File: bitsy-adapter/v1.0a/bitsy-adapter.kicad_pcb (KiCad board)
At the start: 2 copper layers, 63.5 x 31.8 mm, 17 parts, among them J1 PMOD1, J2 PMOD2, J3 PMOD3, J4 5V AUX, J5 5V AUX

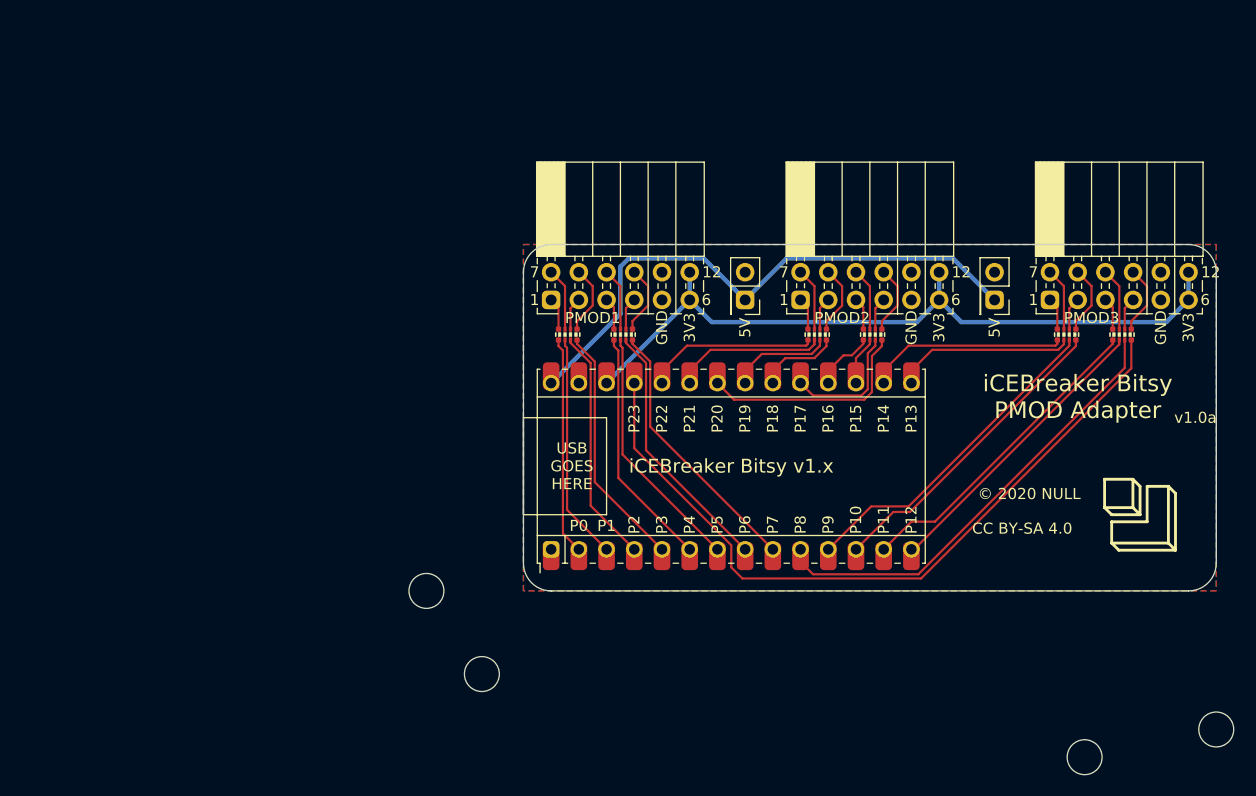
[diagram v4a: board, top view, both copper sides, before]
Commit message: Bitsy Adapter: change formfactor
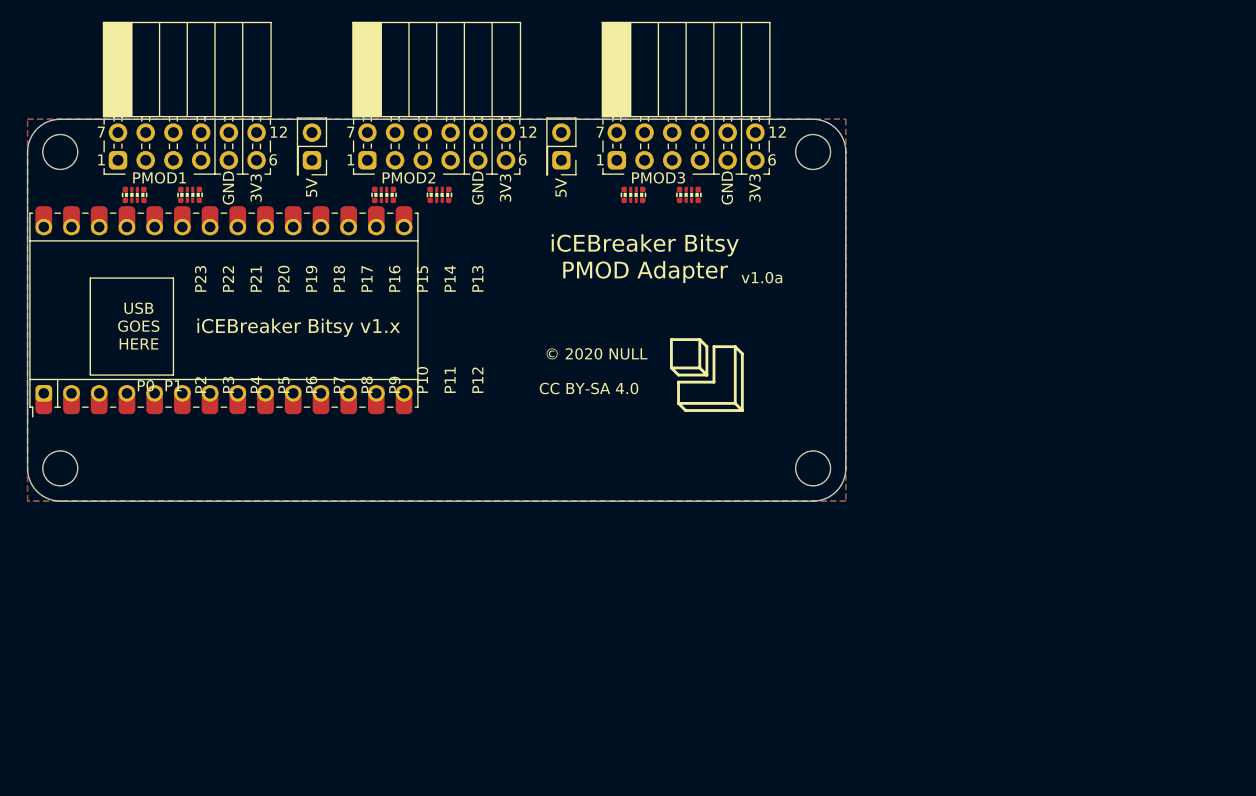
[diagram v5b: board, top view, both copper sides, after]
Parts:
- moved H2 109.0 mm to (65.5, 85.5)
- moved H4 56.7 mm to (134.5, 85.5)
- moved A1 48.6 mm to (80.5, 100.0)
- moved H3 44.0 mm to (134.5, 114.5)
- moved J4 41.7 mm to (88.6, 86.3)
- moved LOGO1 41.7 mm to (124.8, 105.9)
- moved J3 41.7 mm to (116.5, 86.3)
- moved R1 41.7 mm to (72.3, 89.4)
- moved R4 41.7 mm to (100.3, 89.4)
- moved R5 41.7 mm to (118.0, 89.4)
- moved J1 41.7 mm to (70.8, 86.3)
- moved J2 41.7 mm to (93.7, 86.3)
- moved J5 41.7 mm to (111.4, 86.3)
- moved R2 41.7 mm to (77.4, 89.4)
- moved R3 41.7 mm to (95.2, 89.4)
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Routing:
- net /P23: track 68.2 -> 0.00 mm
- net +3V3: track 67.5 -> 0.00 mm
- net +5V: track 52.6 -> 0.00 mm
- net /P8: track 41.1 -> 0.00 mm
- net /P9: track 30.3 -> 0.00 mm
- net /P11: track 29.1 -> 0.00 mm
- net /P10: track 28.4 -> 0.00 mm
- net /P12: track 27.2 -> 0.00 mm
- net /P7: track 24.5 -> 0.00 mm
- net /P6: track 23.7 -> 0.00 mm
- net /P5: track 22.9 -> 0.00 mm
- net /P3: track 22.4 -> 0.00 mm
- net /P4: track 22.1 -> 0.00 mm
- net /P2: track 21.6 -> 0.00 mm
- net /P1: track 20.8 -> 0.00 mm
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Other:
- board size 63.5 x 31.8 mm -> 75 x 35 mm

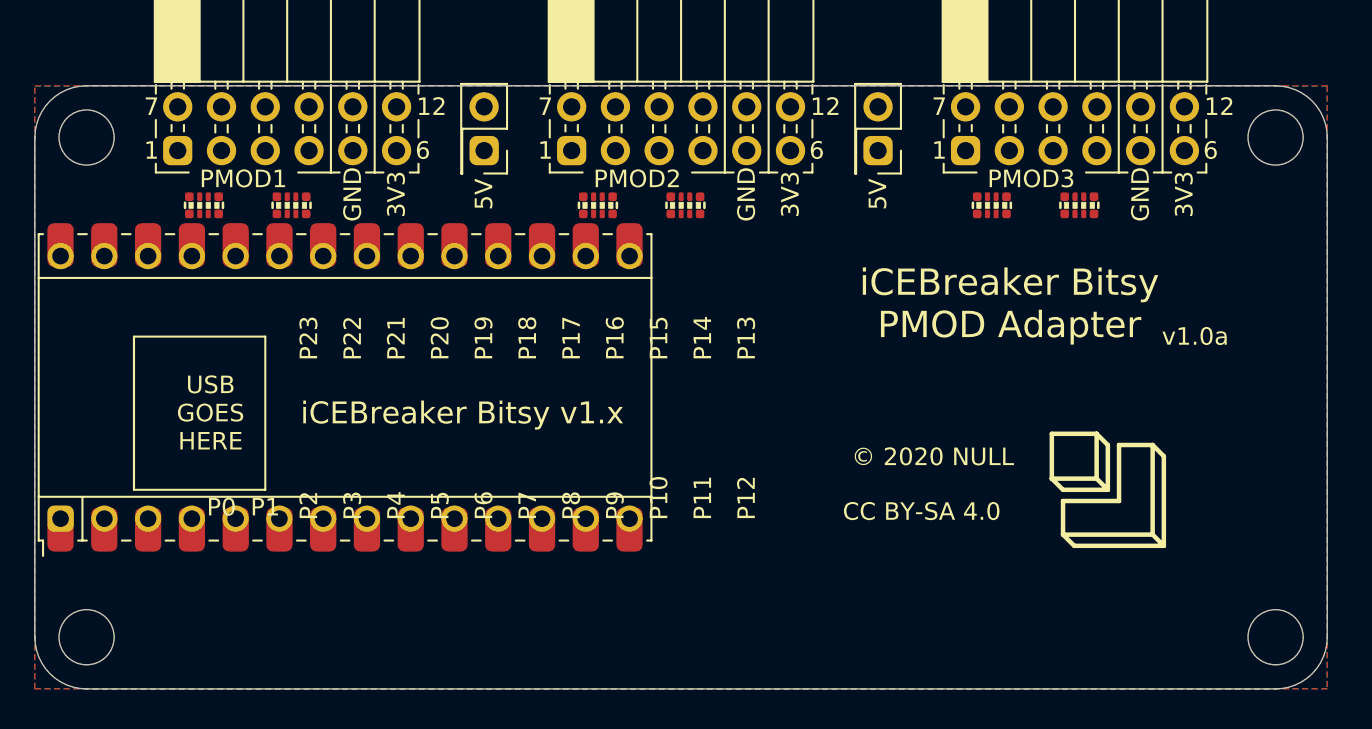
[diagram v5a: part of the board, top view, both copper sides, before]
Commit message: Bitsy Adapter: finish v1.0a
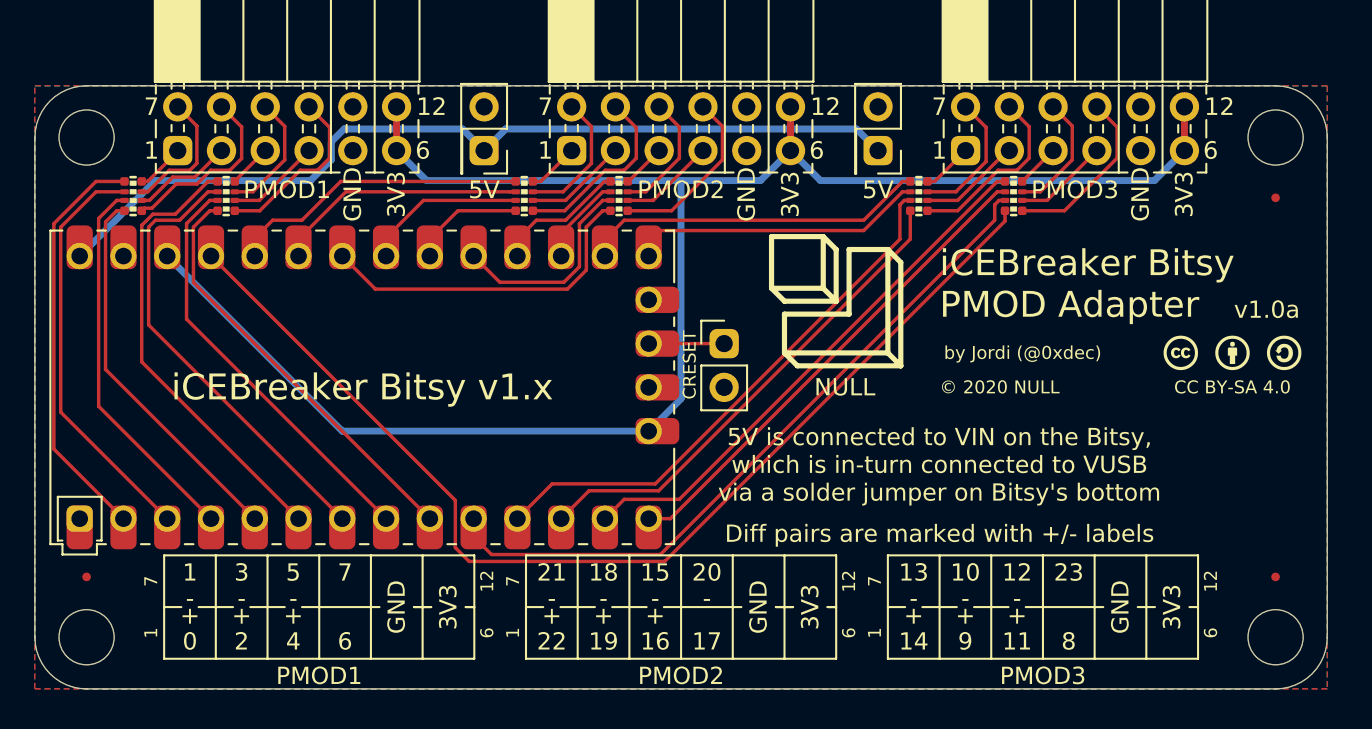
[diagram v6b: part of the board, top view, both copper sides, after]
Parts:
- added FID1: Fiducial, Fiducial:Fiducial_0.5mm_Mask1.5mm, F.Cu at (65.5, 111.0)
- added FID2: Fiducial, Fiducial:Fiducial_0.5mm_Mask1.5mm, F.Cu at (134.5, 111.0)
- added FID3: Fiducial, Fiducial:Fiducial_0.5mm_Mask1.5mm, F.Cu at (134.5, 89.0)
- added JP1: CRESET, Connector_PinHeader_2.54mm:PinHeader_1x02_P2.54mm_Vertical, F.Cu at (102.5, 97.5)
- added REF**: 1b2_Logo_SilkS_7.5mm, pkl_logos:1b2_Logo_SilkS_7.5mm, B.Cu at (132.0, 95.0)
- added REF**: Symbol_CC-SA_SilkScreen_2mm, pkl_logos:Symbol_CC-SA_SilkScreen_2mm, B.Cu at (106.0, 98.0)
- added REF**: Symbol_CC-BY_SilkScreen_2mm, pkl_logos:Symbol_CC-BY_SilkScreen_2mm, B.Cu at (109.0, 98.0)
- added REF**: Symbol_CC_SilkScreen_2mm, pkl_logos:Symbol_CC_SilkScreen_2mm, B.Cu at (112.0, 98.0)
- added REF**: Symbol_CC-SA_SilkScreen_2mm, pkl_logos:Symbol_CC-SA_SilkScreen_2mm, F.Cu at (135.0, 98.0)
- added REF**: Symbol_CC-BY_SilkScreen_2mm, pkl_logos:Symbol_CC-BY_SilkScreen_2mm, F.Cu at (132.0, 98.0)
- added REF**: Symbol_CC_SilkScreen_2mm, pkl_logos:Symbol_CC_SilkScreen_2mm, F.Cu at (129.0, 98.0)
- LOGO1: footprint pkl_logos:1b2_Logo_SilkS_6.5mm -> pkl_logos:1b2_Logo_SilkS_7.5mm
- moved LOGO1 19.2 mm to (109.0, 95.0)
- moved R3 4.31 mm to (90.9, 88.9), turned to 0 degrees
- moved R5 4.27 mm to (113.8, 88.9), turned to 0 degrees
- moved R1 4.15 mm to (68.2, 88.9), turned to 0 degrees
- moved R4 3.89 mm to (96.4, 88.9), turned to 0 degrees
- moved R6 3.85 mm to (119.3, 88.9), turned to 0 degrees
- moved R2 3.83 mm to (73.6, 88.9), turned to 0 degrees
- moved A1 1.00 mm to (81.5, 100.0)
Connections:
- A1 pad 15: /P13 -> +3V3
- A1 pad 16: /P14 -> GND
- A1 pad 17: /P15 -> /CRESET
- A1 pad 18: /P16 -> /CDONE
- A1 pad 19: /P17 -> /P13
- A1 pad 20: /P18 -> /P14
- A1 pad 21: /P19 -> /P15
- A1 pad 22: /P20 -> /P16
- A1 pad 23: /P21 -> /P17
- A1 pad 24: /P22 -> /P18
- A1 pad 25: /P23 -> /P19
- A1 pad 26: +3V3 -> /P20
- A1 pad 27: GND -> /P21
- A1 pad 28: +5V -> /P22
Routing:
- net +3V3: track 0.00 -> 103.7 mm
- net /P23: track 0.00 -> 63.8 mm
- net +5V: track 0.00 -> 51.6 mm
- net /P8: track 0.00 -> 40.8 mm
- net /P9: track 0.00 -> 31.6 mm
- net /P11: track 0.00 -> 31.3 mm
- net /P10: track 0.00 -> 28.6 mm
- net /P12: track 0.00 -> 28.5 mm
- net /P5: track 0.00 -> 26.4 mm
- net /P4: track 0.00 -> 26.2 mm
- net /P7: track 0.00 -> 24.4 mm
- net /P6: track 0.00 -> 24.3 mm
- net /P1: track 0.00 -> 24.0 mm
- net /P0: track 0.00 -> 23.9 mm
- net /P3: track 0.00 -> 22.2 mm
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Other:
- net class Default: clearance 0.1524 -> 0.15; trace_width 0.2032 -> 0.2; via_dia 0.6096 -> 0.6; via_drill 0.3048 -> 0.3
- net class Power: clearance 0.1524 -> 0.15; trace_width 0.4064 -> 0.4; via_dia 0.6096 -> 0.6; via_drill 0.3048 -> 0.3
- rule pad_to_mask_clearance: 0.05 -> 0
- rule trace_clearance: 0.1524 -> 0.15
- rule trace_min: 0.1524 -> 0.15
- rule via_min_drill: 0.254 -> 0.25
- rule via_min_size: 0.4572 -> 0.5
- board text added: "+"
- board text added: "-"
- board text added: "0"
- board text added: "10"
- board text added: "11"
- board text added: "13"
- board text added: "14"
- board text added: "15"
- board text added: "16"
- board text added: "17"
- board text added: "18"
- board text added: "19"
- board text added: "2"
- board text added: "20"
- board text added: "21"
- board text added: "22"
- board text added: "23"
- board text added: "3"
- board text added: "4"
- board text added: "5"
- board text added: "5V is connected to VIN on the Bitsy, which is in-turn connected to VUSB via a solder jumper on Bitsy's bottom"
- board text added: "8"
- board text added: "9"
- board text added: "CRESET"
- board text added: "Diff pairs are marked with +/- labels"
- board text added: "NULL"
- board text added: "by Jordi (@0xdec)"
- board text removed: "5V is connected to VIN on the Bitsy, which is in turn jumpered to VUSB"
- board text removed: "P1A1"
- board text removed: "P1A10"
- board text removed: "P1A2"
- board text removed: "P1A3"
- board text removed: "P1A4"
- board text removed: "P1A7"
- board text removed: "P1A8"
- board text removed: "P1A9"
- board text removed: "P1B1"
- board text removed: "P1B10"
- board text removed: "P1B2"
- board text removed: "P1B3"
- board text removed: "P1B4"
- board text removed: "P1B7"
- board text removed: "P1B8"
- board text removed: "P1B9"
- board text removed: "P2_1"
- board text removed: "P2_10"
- board text removed: "P2_2"
- board text removed: "P2_3"
- board text removed: "P2_4"
- board text removed: "P2_7"
- board text removed: "P2_8"
- board text removed: "P2_9"
- board text removed: "PMOD1A"
- board text removed: "PMOD1B"
- board text removed: "USB GOES HERE"
- board text removed: "iCEBreaker Bitsy PMOD Adapter v1.0a"
- board text removed: "© 2020 NULL CC BY-SA 4.0"

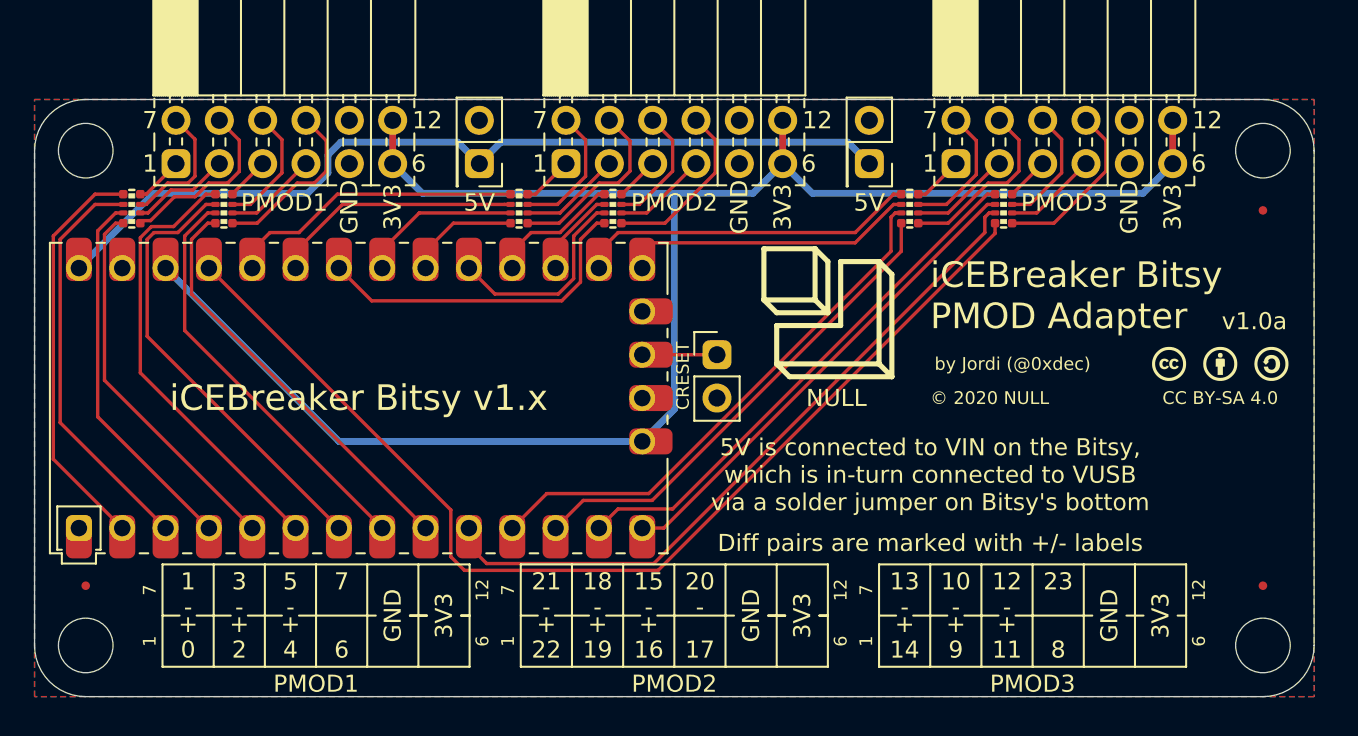
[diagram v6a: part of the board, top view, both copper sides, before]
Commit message: Bitsy Adapter: finish v1.0a for real this time
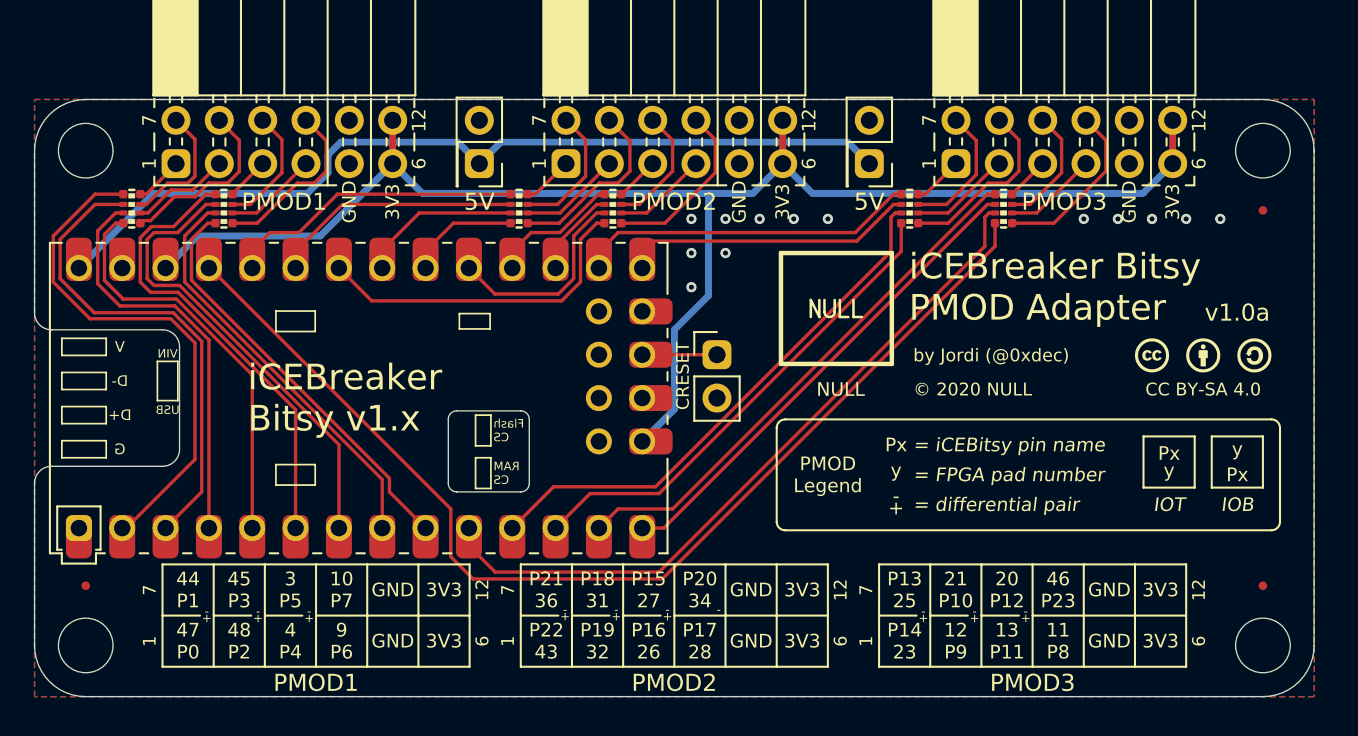
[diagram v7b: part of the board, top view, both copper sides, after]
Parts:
- LOGO1: footprint pkl_logos:1b2_Logo_SilkS_7.5mm -> pkl_logos:null_Logo_SilkS_6.5mm
- REF**: value 1b2_Logo_SilkS_7.5mm -> null_Logo_SilkS_6.5mm; footprint pkl_logos:1b2_Logo_SilkS_7.5mm -> pkl_logos:null_Logo_SilkS_6.5mm
- moved REF** 1.58 mm to (107.5, 97.5)
- moved REF** 1.58 mm to (110.5, 97.5)
- moved REF** 1.58 mm to (113.5, 97.5)
- moved REF** 1.12 mm to (134.0, 97.5)
- moved REF** 1.12 mm to (131.0, 97.5)
- moved REF** 1.12 mm to (128.0, 97.5)
- moved LOGO1 0.56 mm to (109.5, 94.8)
- moved REF** 0.25 mm to (132.0, 94.8)
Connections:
- A1 pad 15: +3V3 -> /P13
- A1 pad 16: GND -> /P14
- A1 pad 17: /CRESET -> /P15
- A1 pad 18: /CDONE -> /P16
- A1 pad 19: /P13 -> /P17
- A1 pad 20: /P14 -> /P18
- A1 pad 21: /P15 -> /P19
- A1 pad 22: /P16 -> /P20
- A1 pad 23: /P17 -> /P21
- A1 pad 24: /P18 -> /P22
- A1 pad 25: /P19 -> /P23
- A1 pad 26: /P20 -> +3V3
- A1 pad 27: /P21 -> GND
- A1 pad 28: /P22 -> +5V
- A1 pad 29: /P23 -> +3V3
- A1 pad 30: +3V3 -> GND
- A1 pad 31: GND -> /CRESET
- A1 pad 32: +5V -> /CDONE
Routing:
- net +3V3: track 103.7 -> 88.2 mm
- net /P0: track 23.9 -> 30.4 mm
- net /P1: track 24.0 -> 28.5 mm
- net /P2: track 22.1 -> 23.9 mm
- net /P3: track 22.2 -> 24.0 mm
- net /P4: track 26.2 -> 27.2 mm
- net /P23: track 63.8 -> 64.7 mm
- net /P5: track 26.4 -> 27.3 mm
- net /P8: track 40.8 -> 41.7 mm
- net GND: vias 0 -> 13
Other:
- outline, holes or cut-outs redrawn
- board text added: "10 P7"
- board text added: "11 P8"
- board text added: "12 P9"
- board text added: "13 P11"
- board text added: "20 P12"
- board text added: "21 P10"
- board text added: "3 P5"
- board text added: "4 P4"
- board text added: "44 P1"
- board text added: "45 P3"
- board text added: "46 P23"
- board text added: "47 P0"
- board text added: "48 P2"
- board text added: "9 P6"
- board text added: "= FPGA pad number"
- board text added: "= differential pair"
- board text added: "= iCEBitsy pin name"
- board text added: "Aux. 5Volt Power Diagram"
- board text added: "CDONE"
- board text added: "CIPO"
- board text added: "COPI"
- board text added: "CRST"
- board text added: "CS"
- board text added: "IOB"
- board text added: "IOT"
- board text added: "P13 25"
- board text added: "P14 23"
- board text added: "P15 27"
- board text added: "P16 26"
- board text added: "P17 28"
- board text added: "P18 31"
- board text added: "P19 32"
- board text added: "P20 34"
- board text added: "P21 36"
- board text added: "P22 43"
- board text added: "PMOD Legend"
- board text added: "Px"
- board text added: "SCK"
- board text added: "USB"
- board text added: "y"
- board text removed: "0"
- board text removed: "10"
- board text removed: "11"
- board text removed: "13"
- board text removed: "14"
- board text removed: "15"
- board text removed: "16"
- board text removed: "17"
- board text removed: "18"
- board text removed: "19"
- board text removed: "2"
- board text removed: "20"
- board text removed: "21"
- board text removed: "22"
- board text removed: "23"
- board text removed: "3"
- board text removed: "4"
- board text removed: "5"
- board text removed: "5V is connected to VIN on the Bitsy, which is in-turn connected to VUSB via a solder jumper on Bitsy's bottom"
- board text removed: "8"
- board text removed: "9"
- board text removed: "Diff pairs are marked with +/- labels"
